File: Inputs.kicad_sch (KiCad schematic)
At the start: 3 parts, among them J6 inputs, J7 inputs, U4 MCP23017_SP

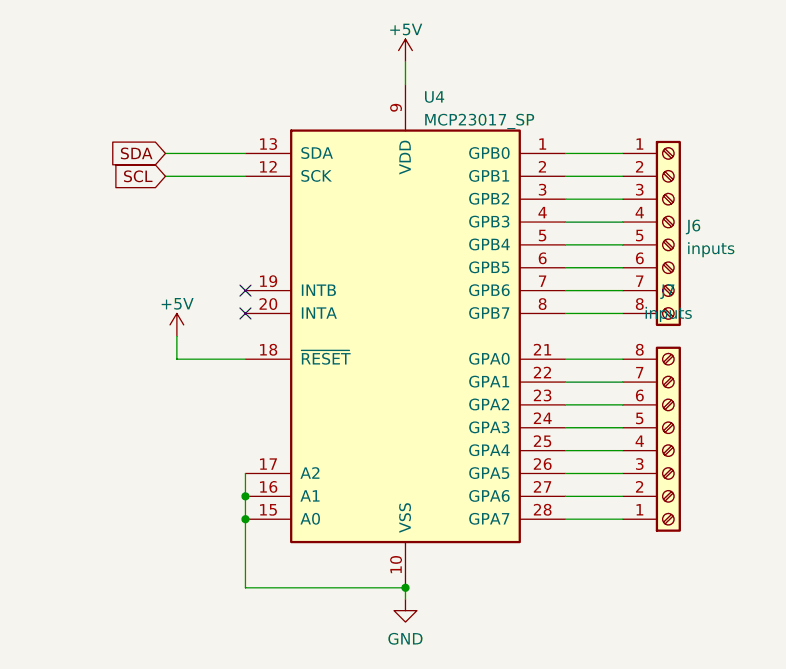
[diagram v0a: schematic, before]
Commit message: redone the switch connectors to accomodate a current sense print. Rearranged parts and updated silk texts to be 50% of their original size
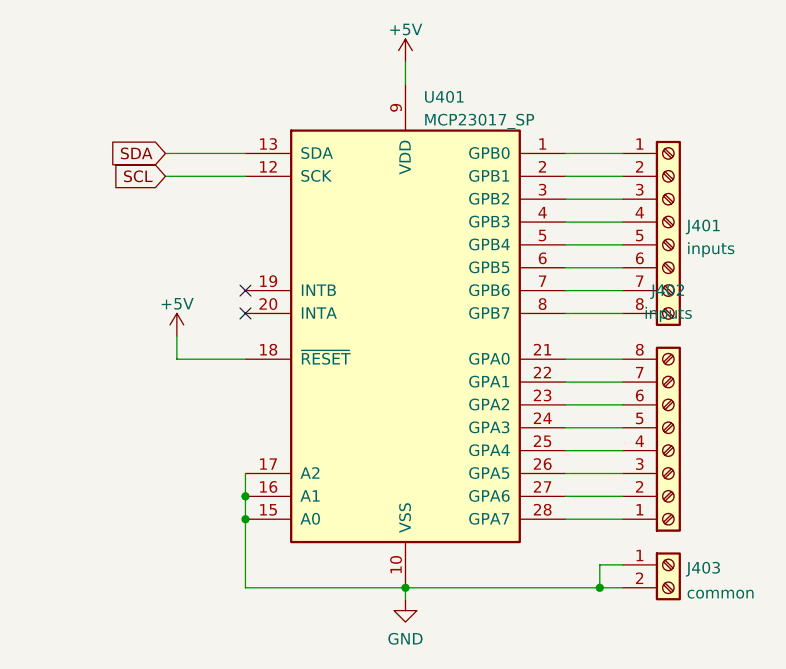
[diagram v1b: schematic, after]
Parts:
- added J403: common, TerminalBlock_Phoenix:TerminalBlock_Phoenix_MPT-0,5-2-2.54_1x02_P2.54mm_Horizontal, symbol Connector:Screw_Terminal_01x02
- U401: renamed from U4; footprint Package_DIP:DIP-28_W7.62mm -> Package_DIP:DIP-28_W7.62mm_Socket
- renumbered J6 to J401, J7 to J402
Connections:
- net GND: now also J403.1 (Pin_1), J403.2 (Pin_2)
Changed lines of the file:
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@@
   (junction (at 134.62 114.3) (diameter 0) (color 0 0 0 0)
+  )
+  (junction (at 173.99 124.46) (diameter 0) (color 0 0 0 0)
   )
   (junction (at 134.62 116.84) (diameter 0) (color 0 0 0 0)
@@
     (stroke (width 0) (type default) (color 0 0 0 0))
   )
+  (wire (pts (xy 173.99 121.92) (xy 173.99 124.46))
+    (stroke (width 0) (type default) (color 0 0 0 0))
+  )
   (wire (pts (xy 127 99.06) (xy 134.62 99.06))
     (stroke (width 0) (type default) (color 0 0 0 0))
@@
     (stroke (width 0) (type default) (color 0 0 0 0))
   )
+  (wire (pts (xy 152.4 124.46) (xy 173.99 124.46))
+    (stroke (width 0) (type default) (color 0 0 0 0))
+  )
   (wire (pts (xy 170.18 76.2) (xy 176.53 76.2))
     (stroke (width 0) (type default) (color 0 0 0 0))
@@
     (stroke (width 0) (type default) (color 0 0 0 0))
   )
+  (wire (pts (xy 176.53 121.92) (xy 173.99 121.92))
+    (stroke (width 0) (type default) (color 0 0 0 0))
+  )
   (wire (pts (xy 170.18 93.98) (xy 176.53 93.98))
     (stroke (width 0) (type default) (color 0 0 0 0))
@@
   )
   (wire (pts (xy 170.18 81.28) (xy 176.53 81.28))
+    (stroke (width 0) (type default) (color 0 0 0 0))
+  )
+  (wire (pts (xy 173.99 124.46) (xy 176.53 124.46))
     (stroke (width 0) (type default) (color 0 0 0 0))
   )
@@
   (symbol (lib_id "power:GND") (at 152.4 125.73 0) (unit 1)
     (in_bom yes) (on_board yes) (fields_autoplaced)
-    (property "Reference" "#PWR0131" (id 0) (at 152.4 132.08 0)
+    (property "Reference" "#PWR0403" (id 0) (at 152.4 132.08 0)
       (effects (font (size 1.27 1.27)) hide)
     )
@@
   (symbol (lib_id "power:+5V") (at 127 96.52 0) (unit 1)
     (in_bom yes) (on_board yes) (fields_autoplaced)
-    (property "Reference" "#PWR0130" (id 0) (at 127 100.33 0)
+    (property "Reference" "#PWR0401" (id 0) (at 127 100.33 0)
       (effects (font (size 1.27 1.27)) hide)
     )
@@
   (symbol (lib_id "Connector:Screw_Terminal_01x08") (at 181.61 83.82 0) (unit 1)
     (in_bom yes) (on_board yes) (fields_autoplaced)
-    (property "Reference" "J6" (id 0) (at 183.642 84.2553 0)
+    (property "Reference" "J401" (id 0) (at 183.642 84.2553 0)
       (effects (font (size 1.27 1.27)) (justify left))
     )
@@
     (pin "8")
   )
+  (symbol (lib_id "Connector:Screw_Terminal_01x02") (at 181.61 121.92 0) (unit 1)
+    (in_bom yes) (on_board yes) (fields_autoplaced)
+    (property "Reference" "J403" (id 0) (at 183.642 122.2815 0)
+      (effects (font (size 1.27 1.27)) (justify left))
+    )
+    (property "Value" "common" (id 1) (at 183.642 125.0566 0)
+      (effects (font (size 1.27 1.27)) (justify left))
+    )
+    (property "Footprint" "TerminalBlock_Phoenix:TerminalBlock_Phoenix_MPT-0,5-2-2.54_1x02_P2.54mm_Horizontal" (id 2) (at 181.61 121.92 0)
+      (effects (font (size 1.27 1.27)) hide)
+    )
+    (property "Datasheet" "~" (id 3) (at 181.61 121.92 0)
+      (effects (font (size 1.27 1.27)) hide)
+    )
+    (pin "1")
+    (pin "2")
+  )
   (symbol (lib_id "power:+5V") (at 152.4 66.04 0) (unit 1)
     (in_bom yes) (on_board yes) (fields_autoplaced)
-    (property "Reference" "#PWR0129" (id 0) (at 152.4 69.85 0)
+    (property "Reference" "#PWR0402" (id 0) (at 152.4 69.85 0)
       (effects (font (size 1.27 1.27)) hide)
     )
@@
   (symbol (lib_id "Connector:Screw_Terminal_01x08") (at 181.61 109.22 0) (mirror x) (unit 1)
     (in_bom yes) (on_board yes)
-    (property "Reference" "J7" (id 0) (at 181.61 91.44 0))
+    (property "Reference" "J402" (id 0) (at 181.61 91.44 0))
     (property "Value" "inputs" (id 1) (at 181.61 93.98 0))
     (property "Footprint" "TerminalBlock_Phoenix:TerminalBlock_Phoenix_MPT-0,5-8-2.54_1x08_P2.54mm_Horizontal" (id 2) (at 181.61 109.22 0)
@@
   (symbol (lib_id "Interface_Expansion:MCP23017_SP") (at 152.4 96.52 0) (unit 1)
     (in_bom yes) (on_board yes) (fields_autoplaced)
-    (property "Reference" "U4" (id 0) (at 154.4194 69.9602 0)
+    (property "Reference" "U401" (id 0) (at 154.4194 69.9602 0)
       (effects (font (size 1.27 1.27)) (justify left))
     )
@@
       (effects (font (size 1.27 1.27)) (justify left))
     )
-    (property "Footprint" "Package_DIP:DIP-28_W7.62mm" (id 2) (at 157.48 121.92 0)
+    (property "Footprint" "Package_DIP:DIP-28_W7.62mm_Socket" (id 2) (at 157.48 121.92 0)
       (effects (font (size 1.27 1.27)) (justify left) hide)
     )

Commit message: I have a problem that I lose the links between symbols and footprints. I want to add a spst switch to connect the bus' voltage to the main power
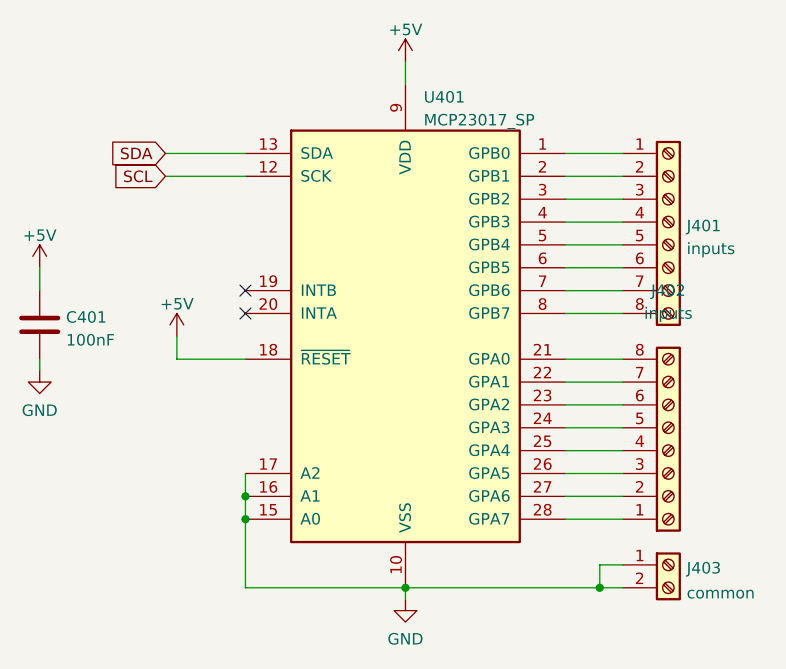
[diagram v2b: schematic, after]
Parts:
- added C401: 100nF, Capacitor_THT:C_Disc_D3.0mm_W1.6mm_P2.50mm, symbol Device:C
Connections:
- net +5V: now also C401.1
- net GND: now also C401.2
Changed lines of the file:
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@@
+    (stroke (width 0) (type default) (color 0 0 0 0))
+  )
+  (wire (pts (xy 111.76 99.06) (xy 111.76 100.33))
     (stroke (width 0) (type default) (color 0 0 0 0))
   )
@@
   )
   (wire (pts (xy 170.18 76.2) (xy 176.53 76.2))
+    (stroke (width 0) (type default) (color 0 0 0 0))
+  )
+  (wire (pts (xy 111.76 88.9) (xy 111.76 91.44))
     (stroke (width 0) (type default) (color 0 0 0 0))
   )
@@
   (symbol (lib_id "power:GND") (at 152.4 125.73 0) (unit 1)
     (in_bom yes) (on_board yes) (fields_autoplaced)
-    (property "Reference" "#PWR0403" (id 0) (at 152.4 132.08 0)
+    (property "Reference" "#PWR0405" (id 0) (at 152.4 132.08 0)
       (effects (font (size 1.27 1.27)) hide)
     )
@@
   (symbol (lib_id "power:+5V") (at 127 96.52 0) (unit 1)
     (in_bom yes) (on_board yes) (fields_autoplaced)
-    (property "Reference" "#PWR0401" (id 0) (at 127 100.33 0)
+    (property "Reference" "#PWR0403" (id 0) (at 127 100.33 0)
       (effects (font (size 1.27 1.27)) hide)
     )
@@
     )
     (property "Datasheet" "" (id 3) (at 127 96.52 0)
+      (effects (font (size 1.27 1.27)) hide)
+    )
+    (pin "1")
+  )
+  (symbol (lib_id "power:+5V") (at 111.76 88.9 0) (unit 1)
+    (in_bom yes) (on_board yes) (fields_autoplaced)
+    (property "Reference" "#PWR0401" (id 0) (at 111.76 92.71 0)
+      (effects (font (size 1.27 1.27)) hide)
+    )
+    (property "Value" "+5V" (id 1) (at 111.76 85.3242 0))
+    (property "Footprint" "" (id 2) (at 111.76 88.9 0)
+      (effects (font (size 1.27 1.27)) hide)
+    )
+    (property "Datasheet" "" (id 3) (at 111.76 88.9 0)
       (effects (font (size 1.27 1.27)) hide)
     )
@@
   (symbol (lib_id "power:+5V") (at 152.4 66.04 0) (unit 1)
     (in_bom yes) (on_board yes) (fields_autoplaced)
-    (property "Reference" "#PWR0402" (id 0) (at 152.4 69.85 0)
+    (property "Reference" "#PWR0404" (id 0) (at 152.4 69.85 0)
       (effects (font (size 1.27 1.27)) hide)
     )
@@
     (pin "7")
     (pin "8")
+  )
+  (symbol (lib_id "Device:C") (at 111.76 95.25 0) (unit 1)
+    (in_bom yes) (on_board yes) (fields_autoplaced)
+    (property "Reference" "C401" (id 0) (at 114.681 94.4153 0)
+      (effects (font (size 1.27 1.27)) (justify left))
+    )
+    (property "Value" "100nF" (id 1) (at 114.681 96.9522 0)
+      (effects (font (size 1.27 1.27)) (justify left))
+    )
+    (property "Footprint" "Capacitor_THT:C_Disc_D3.0mm_W1.6mm_P2.50mm" (id 2) (at 112.7252 99.06 0)
+      (effects (font (size 1.27 1.27)) hide)
+    )
+    (property "Datasheet" "~" (id 3) (at 111.76 95.25 0)
+      (effects (font (size 1.27 1.27)) hide)
+    )
+    (pin "1")
+    (pin "2")
   )
   (symbol (lib_id "Interface_Expansion:MCP23017_SP") (at 152.4 96.52 0) (unit 1)
@@
     (pin "9")
   )
+  (symbol (lib_id "power:GND") (at 111.76 100.33 0) (unit 1)
+    (in_bom yes) (on_board yes) (fields_autoplaced)
+    (property "Reference" "#PWR0402" (id 0) (at 111.76 106.68 0)
+      (effects (font (size 1.27 1.27)) hide)
+    )
+    (property "Value" "GND" (id 1) (at 111.76 104.7734 0))
+    (property "Footprint" "" (id 2) (at 111.76 100.33 0)
+      (effects (font (size 1.27 1.27)) hide)
+    )
+    (property "Datasheet" "" (id 3) (at 111.76 100.33 0)
+      (effects (font (size 1.27 1.27)) hide)
+    )
+    (pin "1")
+  )
 )

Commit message: altered the code drastically and made a new PCB. PCB is still much work.
I finally fixed that issue where loco functions and speed were not serviced to the multimaus clients.
The Nx code also has been succesfully tested using the monitor.
MCP bug also has been solded. The bug was in assembleIO.py
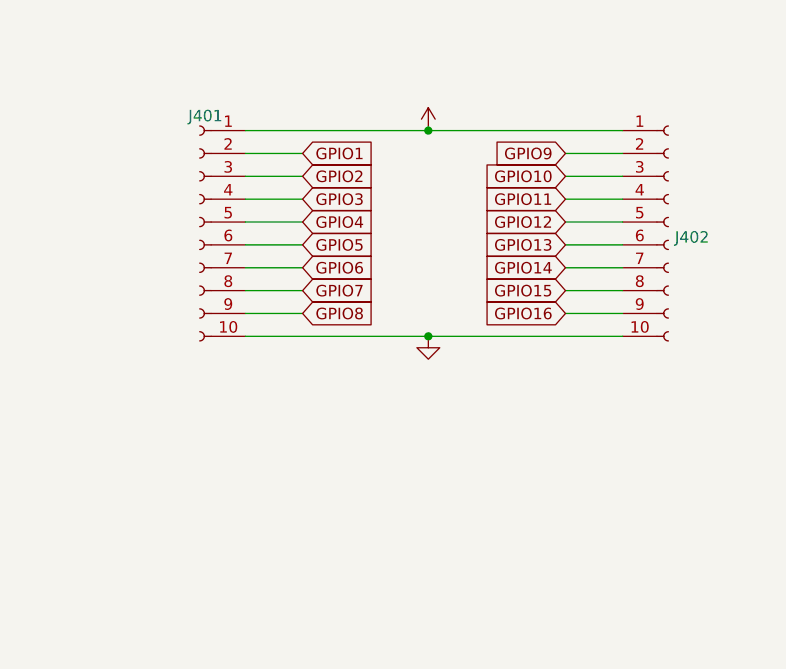
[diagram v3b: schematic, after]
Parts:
- removed C401: 100nF, Capacitor_THT:C_Disc_D3.0mm_W1.6mm_P2.50mm, symbol Device:C
- removed J401, J402: inputs, TerminalBlock_Phoenix:TerminalBlock_Phoenix_MPT-0,5-8-2.54_1x08_P2.54mm_Horizontal, symbol Connector:Screw_Terminal_01x08
- removed J403: common, TerminalBlock_Phoenix:TerminalBlock_Phoenix_MPT-0,5-2-2.54_1x02_P2.54mm_Horizontal, symbol Connector:Screw_Terminal_01x02
- removed U401: MCP23017_SP, Package_DIP:DIP-28_W7.62mm_Socket, symbol Interface_Expansion:MCP23017_SP
- added J401, J402: (no value), symbol Connector:Conn_01x10_Female
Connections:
- net +5V: now also J401.1 (Pin_1), J402.1 (Pin_1)
- net GND: now also J401.10 (Pin_10), J402.10 (Pin_10)
- new net GPIO1: J401.2 (Pin_2)
- new net GPIO10: J402.3 (Pin_3)
- new net GPIO11: J402.4 (Pin_4)
- new net GPIO12: J402.5 (Pin_5)
- new net GPIO13: J402.6 (Pin_6)
- new net GPIO14: J402.7 (Pin_7)
- new net GPIO15: J402.8 (Pin_8)
- new net GPIO16: J402.9 (Pin_9)
- new net GPIO2: J401.3 (Pin_3)
- new net GPIO3: J401.4 (Pin_4)
- new net GPIO4: J401.5 (Pin_5)
- new net GPIO5: J401.6 (Pin_6)
- new net GPIO6: J401.7 (Pin_7)
- new net GPIO7: J401.8 (Pin_8)
- new net GPIO8: J401.9 (Pin_9)
- new net GPIO9: J402.2 (Pin_2)
- no-connect marks 2 -> 0

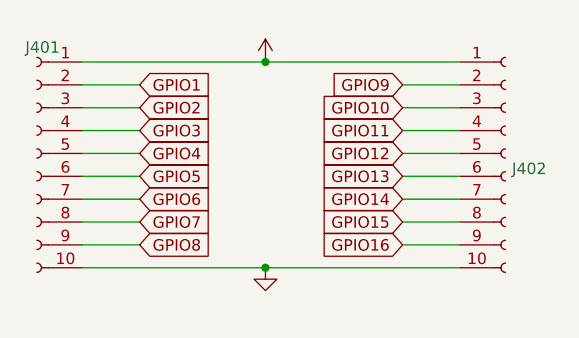
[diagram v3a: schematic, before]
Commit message: added missing schematics
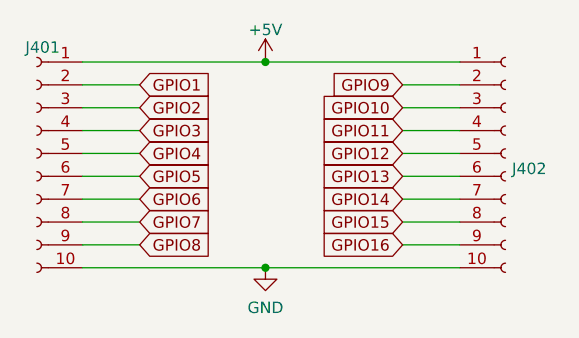
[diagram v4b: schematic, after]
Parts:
- J401, J402: value (none) -> Conn_01x10_Female; footprint (none) -> Connector_PinSocket_2.54mm:PinSocket_1x10_P2.54mm_Horizontal
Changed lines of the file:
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@@
       (effects (font (size 1.27 1.27)) hide)
     )
-    (property "Value" "" (id 1) (at 154.94 70.0842 0))
+    (property "Value" "+5V" (id 1) (at 154.94 70.0842 0))
     (property "Footprint" "" (id 2) (at 154.94 73.66 0)
       (effects (font (size 1.27 1.27)) hide)
@@
     (in_bom yes) (on_board yes) (fields_autoplaced)
     (property "Reference" "J401" (id 0) (at 130.175 72.04 0))
-    (property "Value" "" (id 1) (at 130.175 72.0399 0)
+    (property "Value" "Conn_01x10_Female" (id 1) (at 130.175 72.0399 0)
       (effects (font (size 1.27 1.27)) hide)
     )
-    (property "Footprint" "" (id 2) (at 129.54 83.82 0)
+    (property "Footprint" "Connector_PinSocket_2.54mm:PinSocket_1x10_P2.54mm_Horizontal" (id 2) (at 129.54 83.82 0)
       (effects (font (size 1.27 1.27)) hide)
     )
@@
       (effects (font (size 1.27 1.27)) hide)
     )
-    (property "Value" "" (id 1) (at 154.94 100.9634 0))
+    (property "Value" "GND" (id 1) (at 154.94 100.9634 0))
     (property "Footprint" "" (id 2) (at 154.94 96.52 0)
       (effects (font (size 1.27 1.27)) hide)
@@
       (effects (font (size 1.27 1.27)) (justify left))
     )
-    (property "Value" "" (id 1) (at 182.3212 86.7922 0)
+    (property "Value" "Conn_01x10_Female" (id 1) (at 182.3212 86.7922 0)
       (effects (font (size 1.27 1.27)) (justify left) hide)
     )
-    (property "Footprint" "" (id 2) (at 181.61 83.82 0)
+    (property "Footprint" "Connector_PinSocket_2.54mm:PinSocket_1x10_P2.54mm_Horizontal" (id 2) (at 181.61 83.82 0)
       (effects (font (size 1.27 1.27)) hide)
     )
